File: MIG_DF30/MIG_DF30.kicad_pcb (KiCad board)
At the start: 2 copper layers, 200 x 190 mm, 225 parts, among them K1 G5V-2, K2 G5V-2, Q1 TIC116, Q10 Q_NJFET_SGD, Q11 BC107, Q12 2N3905, Q13 BC107, Q14 BC107, Q2 TIC116, Q3 TIC116, Q5 2N3905, Q6 BC107, Q7 BC107, Q8 2N3905, Q9 BC107, U1 4001, U100 LM317_3PinPackage, U2 4001, U3 4011, U4 LM324, U5 LM324, U6 4001, U7 LM2907N

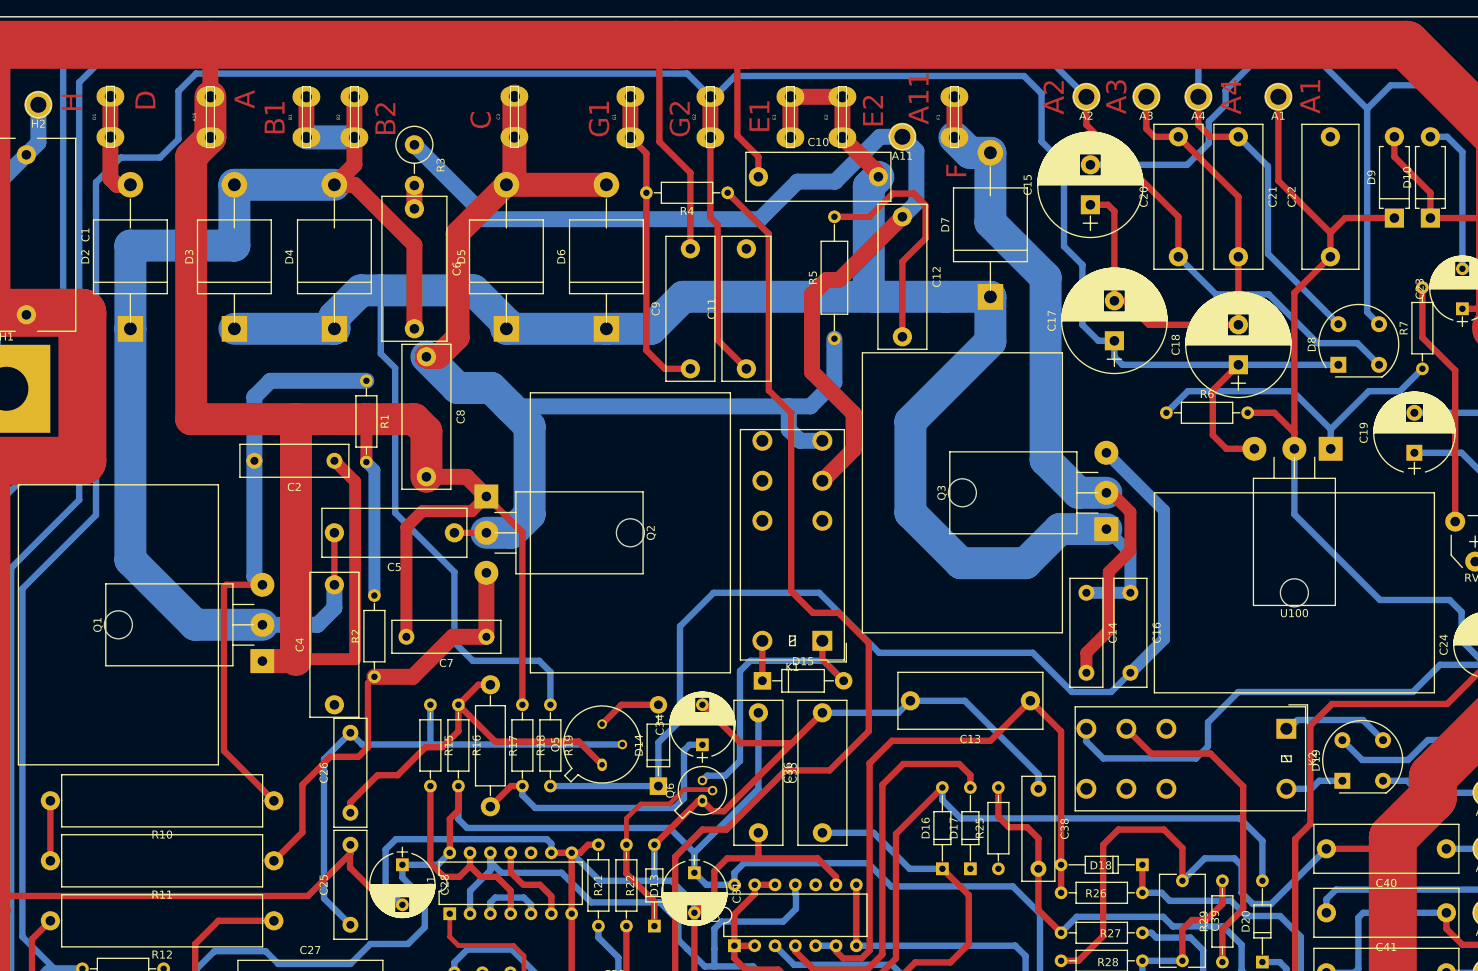
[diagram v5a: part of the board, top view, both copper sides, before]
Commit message: route unconnected
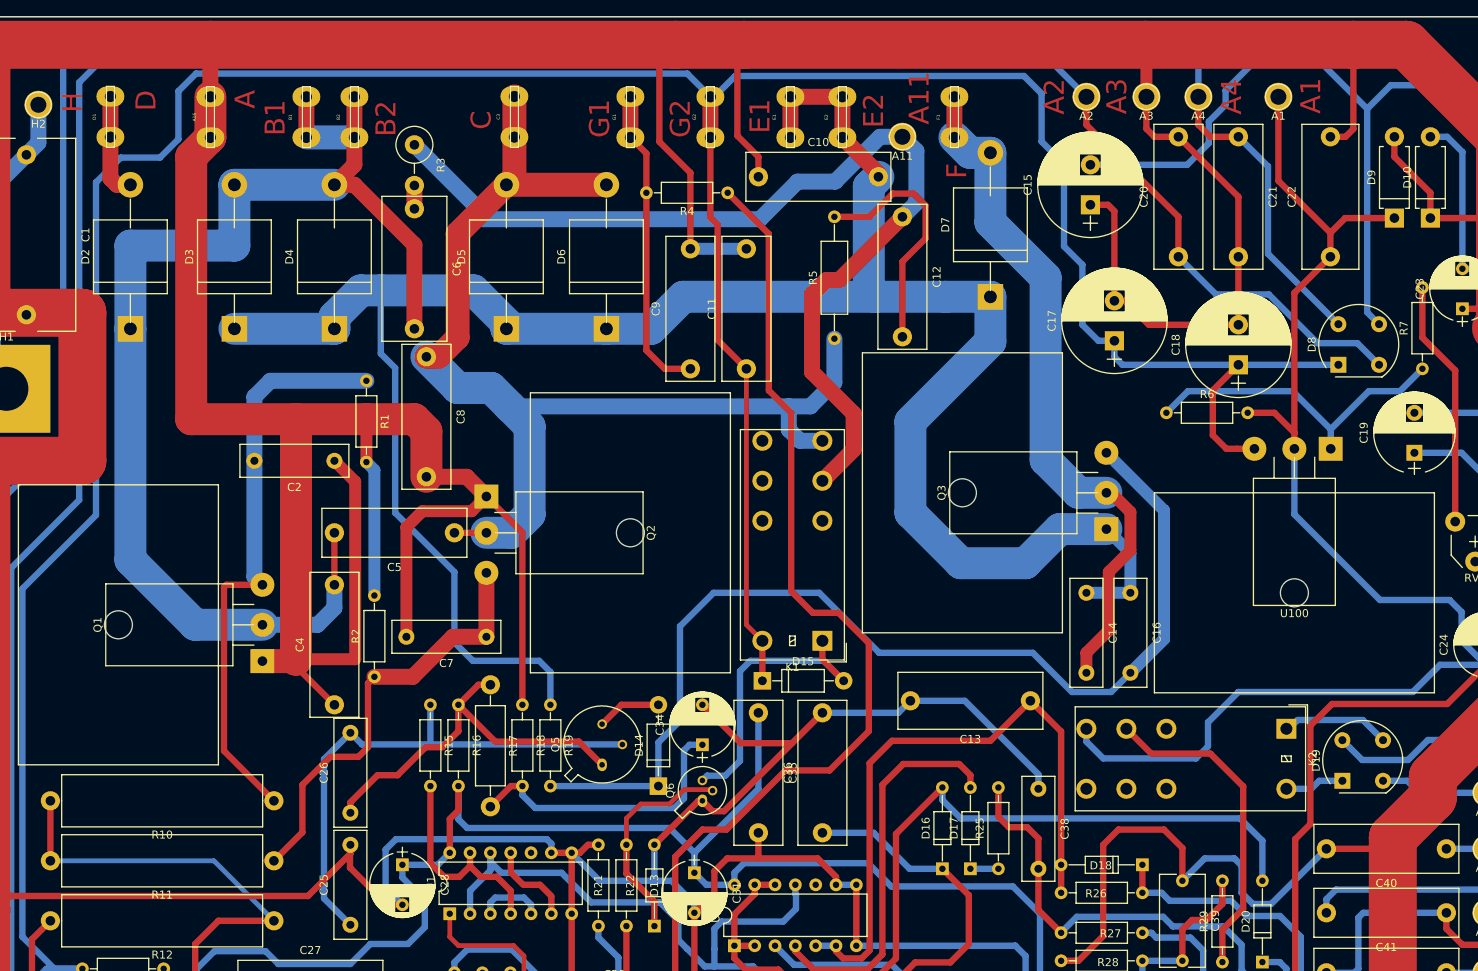
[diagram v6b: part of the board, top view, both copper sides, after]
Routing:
- net GND: track 2147.2 -> 2184.5 mm
- net /G2: track 401.7 -> 436.5 mm
- net Net-(C46-Pad2): track 28.9 -> 60.0 mm
- net Net-(D17-Pad1): track 0.00 -> 3.50 mm
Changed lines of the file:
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@@
     (thickness 1.6)
     (drawings 30)
-    (tracks 1808)
+    (tracks 1824)
     (zones 0)
     (modules 225)
@@
   (page A3)
   (layers
-    (0 F.Cu signal)
+    (0 F.Cu signal hide)
     (31 B.Cu signal)
     (32 B.Adhes user)
@@
     (visible_elements FFFDFF7F)
     (pcbplotparams
-      (layerselection 0x00030_ffffffff)
+      (layerselection 0x010fc_ffffffff)
       (usegerberextensions false)
       (usegerberattributes false)
       (usegerberadvancedattributes false)
       (creategerberjobfile false)
-      (excludeedgelayer true)
+      (excludeedgelayer false)
       (linewidth 0.100000)
       (plotframeref false)
@@
       (drillshape 0)
       (scaleselection 1)
-      (outputdirectory ""))
+      (outputdirectory "Gerber/"))
   )
   (net 0 "")
@@
   (segment (start 86.58 58.43) (end 144.68 58.43) (width 6) (layer F.Cu) (net 3))
   (segment (start 144.68 58.43) (end 153.28 58.43) (width 6) (layer F.Cu) (net 3))
-  (segment (start 153.28 58.43) (end 236.08 58.43) (width 6) (layer F.Cu) (net 3))
   (segment (start 236.08 58.43) (end 247.28 69.63) (width 6) (layer F.Cu) (net 3))
   (segment (start 247.28 69.63) (end 247.58 69.93) (width 6) (layer F.Cu) (net 3))
@@
   (segment (start 155.08 74.93) (end 155.08 72.43) (width 0.8) (layer F.Cu) (net 3))
   (segment (start 155.08 72.43) (end 152.45 69.8) (width 0.8) (layer F.Cu) (net 3))
+  (segment (start 167.32 163.43) (end 164.78 163.43) (width 0.8) (layer B.Cu) (net 3))
+  (segment (start 97.14 135.99) (end 97.14 135.47) (width 0.8) (layer F.Cu) (net 3))
+  (segment (start 102.08 140.93) (end 97.14 135.99) (width 0.8) (layer F.Cu) (net 3))
+  (segment (start 153.58 83.93) (end 146.58 83.93) (width 1.5) (layer B.Cu) (net 3))
+  (segment (start 226.58 69.93) (end 228.47 69.93) (width 0.8) (layer F.Cu) (net 3))
+  (segment (start 228.47 69.93) (end 229.45 68.95) (width 0.8) (layer F.Cu) (net 3))
+  (segment (start 229.45 68.95) (end 229.45 58.43) (width 0.8) (layer F.Cu) (net 3))
+  (segment (start 229.45 58.43) (end 236.08 58.43) (width 6) (layer F.Cu) (net 3))
+  (segment (start 203.58 58.51) (end 203.5 58.43) (width 1.5) (layer F.Cu) (net 3))
+  (segment (start 203.58 64.93) (end 203.58 58.51) (width 1.5) (layer F.Cu) (net 3))
+  (segment (start 153.28 58.43) (end 203.5 58.43) (width 6) (layer F.Cu) (net 3))
+  (segment (start 203.5 58.43) (end 229.45 58.43) (width 6) (layer F.Cu) (net 3))
   (segment (start 210.08 64.93) (end 210.08 68.43) (width 0.8) (layer F.Cu) (net 4) (status 400000))
   (segment (start 211.58 69.93) (end 215.08 69.93) (width 0.8) (layer F.Cu) (net 4) (status 800000))
@@
   (segment (start 200.58 98.43) (end 199.58 97.43) (width 0.8) (layer B.Cu) (net 22))
   (segment (start 215.08 98.43) (end 200.58 98.43) (width 0.8) (layer B.Cu) (net 22))
+  (segment (start 153.58 130.93) (end 153.58 98.93) (width 0.6) (layer F.Cu) (net 22))
+  (segment (start 155.58 132.93) (end 153.58 130.93) (width 0.6) (layer F.Cu) (net 22))
   (segment (start 164.58 79.93) (end 168.98 79.93) (width 0.8) (layer F.Cu) (net 23) (status 400000))
   (segment (start 173.08 85.53) (end 173.08 94.93) (width 0.8) (layer F.Cu) (net 23) (status 800000))
@@
   (segment (start 179.68 208.43) (end 184.08 208.43) (width 0.8) (layer B.Cu) (net 37))
   (segment (start 174.98 213.13) (end 179.68 208.43) (width 0.8) (layer B.Cu) (net 37))
+  (segment (start 87.02 160.43) (end 94.52 167.93) (width 0.6) (layer B.Cu) (net 46))
+  (segment (start 66.58 160.43) (end 87.02 160.43) (width 0.6) (layer B.Cu) (net 46))
   (segment (start 190.08 206.83) (end 187.93 204.68) (width 0.8) (layer B.Cu) (net 52))
   (segment (start 190.08 208.43) (end 190.08 206.83) (width 0.8) (layer B.Cu) (net 52))
   (segment (start 187.93 204.68) (end 176.33 204.68) (width 0.8) (layer B.Cu) (net 52))
   (segment (start 176.33 204.68) (end 171.58 209.43) (width 0.8) (layer B.Cu) (net 52))
+  (segment (start 181.58 161.43) (end 185.08 161.43) (width 0.8) (layer B.Cu) (net 65))
   (segment (start 170.78 202.33) (end 173.38 202.33) (width 0.8) (layer B.Cu) (net 101))
   (segment (start 131.58 201.79863) (end 132.34863 201.03) (width 0.8) (layer B.Cu) (net 101))

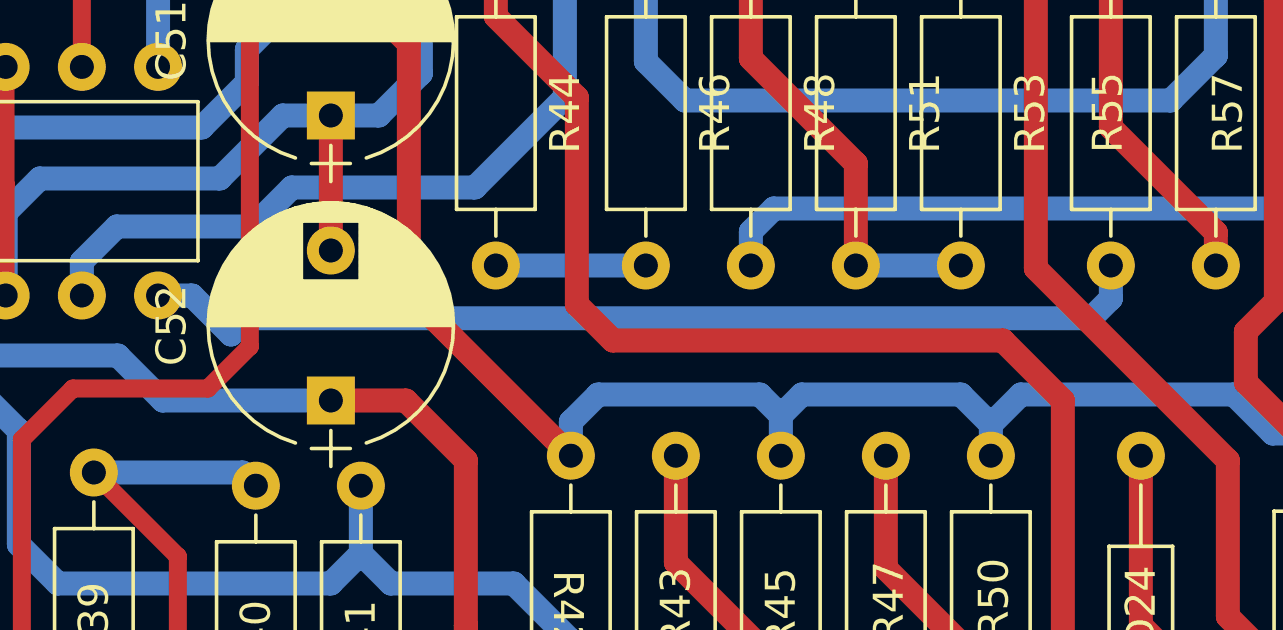
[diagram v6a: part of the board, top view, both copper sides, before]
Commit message: Update component ref
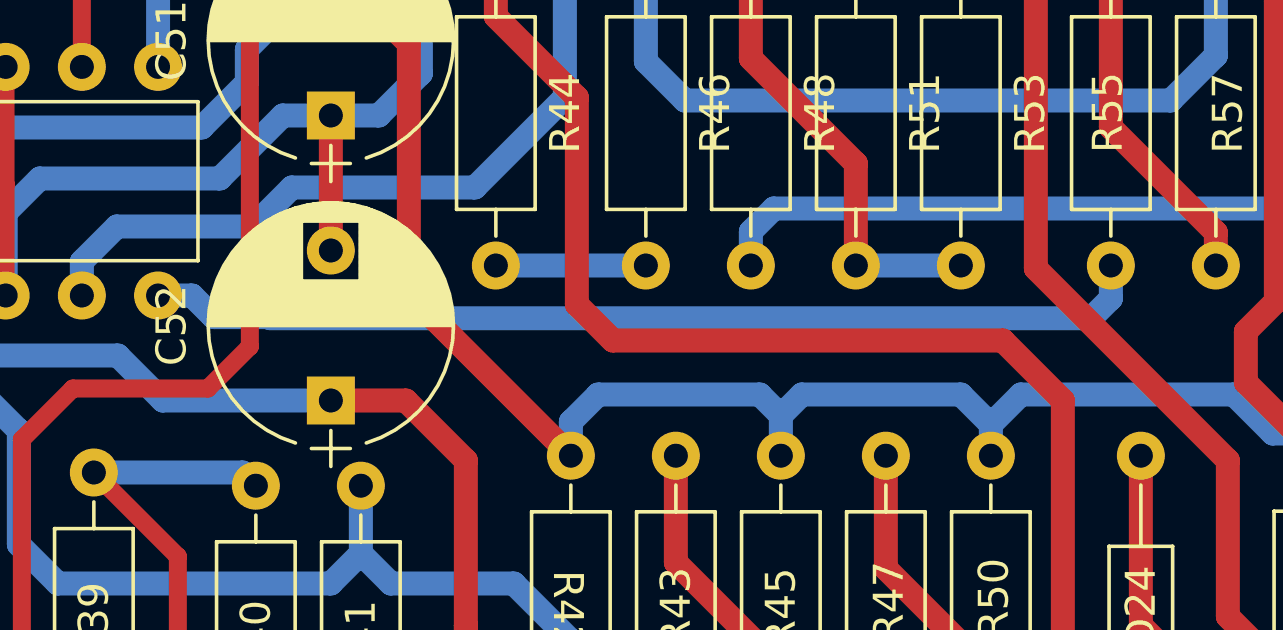
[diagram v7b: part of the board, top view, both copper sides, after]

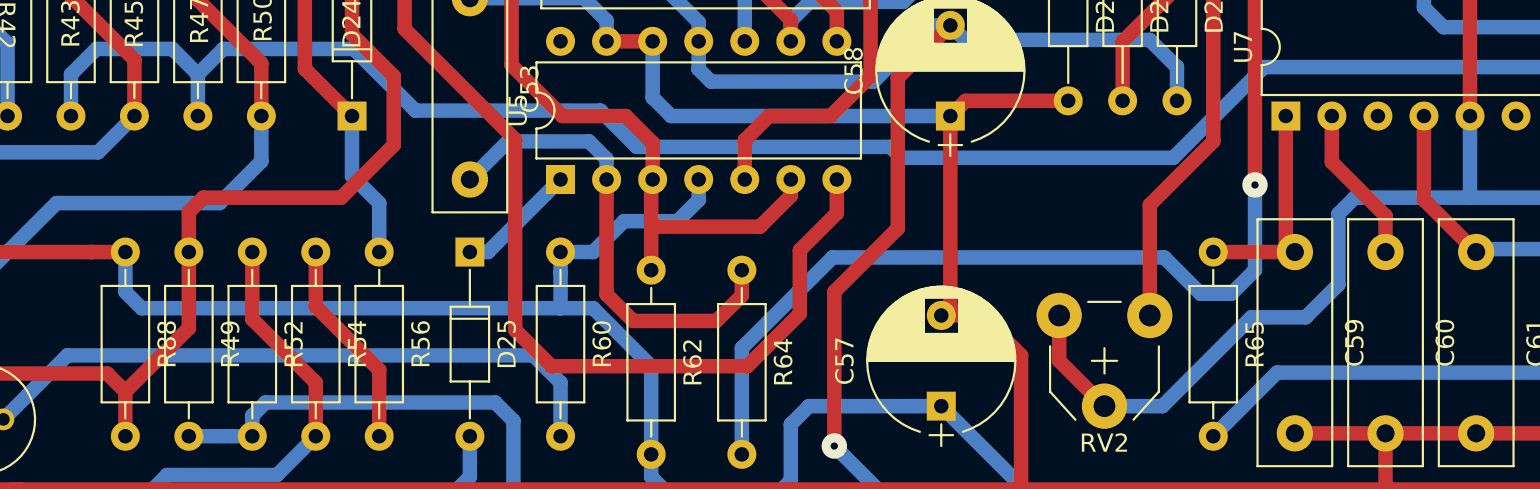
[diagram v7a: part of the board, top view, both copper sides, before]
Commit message: Add missing connection on LM2907 pin 3-4
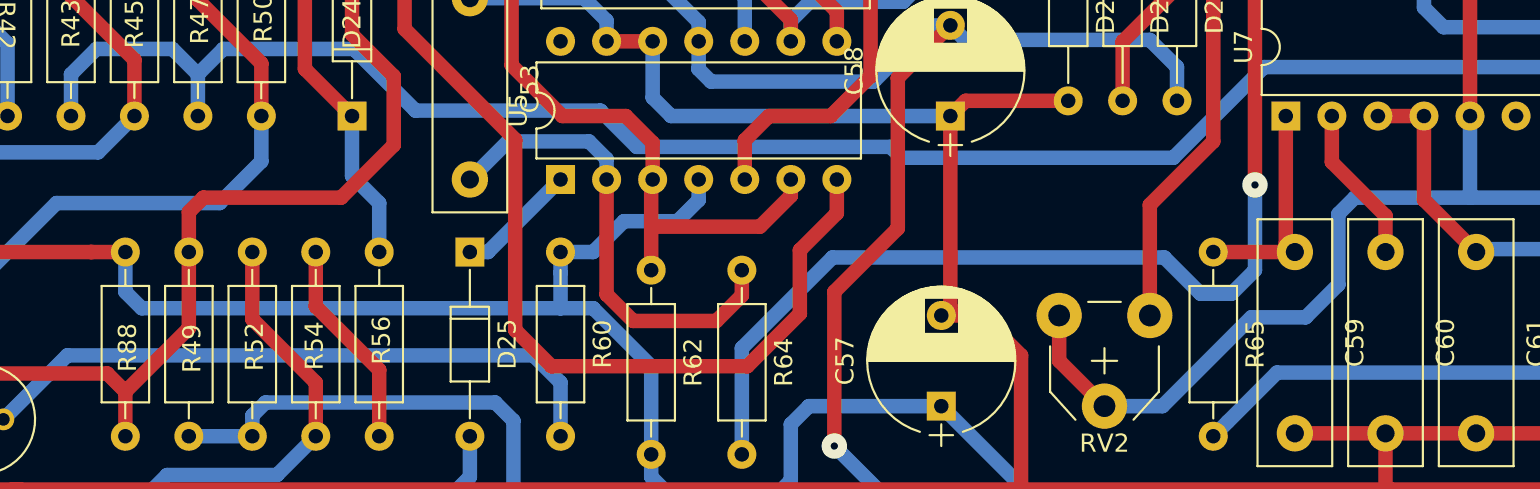
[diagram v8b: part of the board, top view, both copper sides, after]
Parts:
- C10, C11, C20, C21, C35, C40, C41, C42, C43, C67, C68, C69, C70, C8, C9: value C -> 0,1u
- C12: value C -> 0.1u
- C13, C54: value C -> 2.2u
- C14, C16, C2, C25, C29, C32, C33, C44, C45, C47, C48, C49, C50, C55, C59, C61, C7: value C -> 100n
- C19: value CP -> 47u
- C22, C46, C5, C6: value C -> 1u
- C23, C24, C28, C31, C34, C37, C51, C52, C57, C58, C63, C65, C66: value CP -> 10u
- C26, C53, C60: value C -> 10n
- C27, C30: value C -> 680n
- C36: value C -> 1.5u
- C39: value C -> 470n
- C62, C64: value C -> 330n
- D11, D12, D13, D16, D17, D18, D20, D21, D24, D25, D26, D27, D28, D29, D30: value D -> 1N4148
- D19, D8: value D_Bridge_+A-A -> SKB1,2/04
- D2, D3, D4, D5, D6, D7: value D -> MR754
- Q1, Q2, Q3: value TIC116 -> 2N6507
- Q11, Q13, Q14, Q6, Q7, Q9: value BC107 -> BC107A
- Q12: value 2N3905 -> BC177A
- Q5: value 2N3905 -> 2N5415
- Q8: value 2N3905 -> BC161-16
- R1, R19, R2: value R -> 100
- R10, R11: value R -> 220 ohm 5W
- R12: value R -> 270 ohm 5W
- R13: value R -> 680k
- R14, R20: value R -> 330k
- R15, R25, R33, R35, R41, R9: value R -> 1k
- R16, R7: value R -> 2k2
- R17: value R -> 180-1/2W
- R18, R22, R31, R56, R58: value R -> 18k
- R21, R23, R24, R36, R37, R4, R40, R46, R51, R60, R62, R65, R69, R70, R71: value R -> 10k
- R26, R28, R34, R64, R68, R73: value R -> 100k
- R27, R38: value R -> 22k
- R29, R43, R47, R48, R63: value R -> 47k
- R3, R6: value R -> 220
- R30: value R -> 2k2-1/2W
- R32, R59: value R -> 39k
- R39: value R -> 15k
- R42, R45, R50: value R -> 150k
- R44: value R -> 1k25
- R49, R72: value R -> 220k
- R5: value R -> 1k-1/2W
- R52: value R -> 56k
- R53: value R -> 15K
- R54: value R -> 22K
- R55: value R -> 4k7
- R57: value R -> 337
- R61: value R -> 182k
- R66, R67: value R -> 390k
- R8: value R -> 330 ohm 5W
- R88: value R -> NC
- RV1: value R_POT -> 500
- RV2: value R_POT -> 50k
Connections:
- net /-Valim renamed /-15V
- net /A1 renamed /+15V
- U7 pad 3: Net-(U7-Pad3) -> Net-(C61-Pad1)
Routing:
- net Net-(C61-Pad1): track 13.8 -> 16.3 mm
